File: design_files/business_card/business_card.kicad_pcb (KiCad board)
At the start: 2 copper layers, 85 x 55 mm, 35 parts, among them J1 Conn_01x06, J2 Conn_01x04_Male, SW1 SW_Push, SW2 SW_Push, SW3 SW_Push, SW4 SW_Push, U1 ATTINY85-20SU, U2 TLC5940PWP

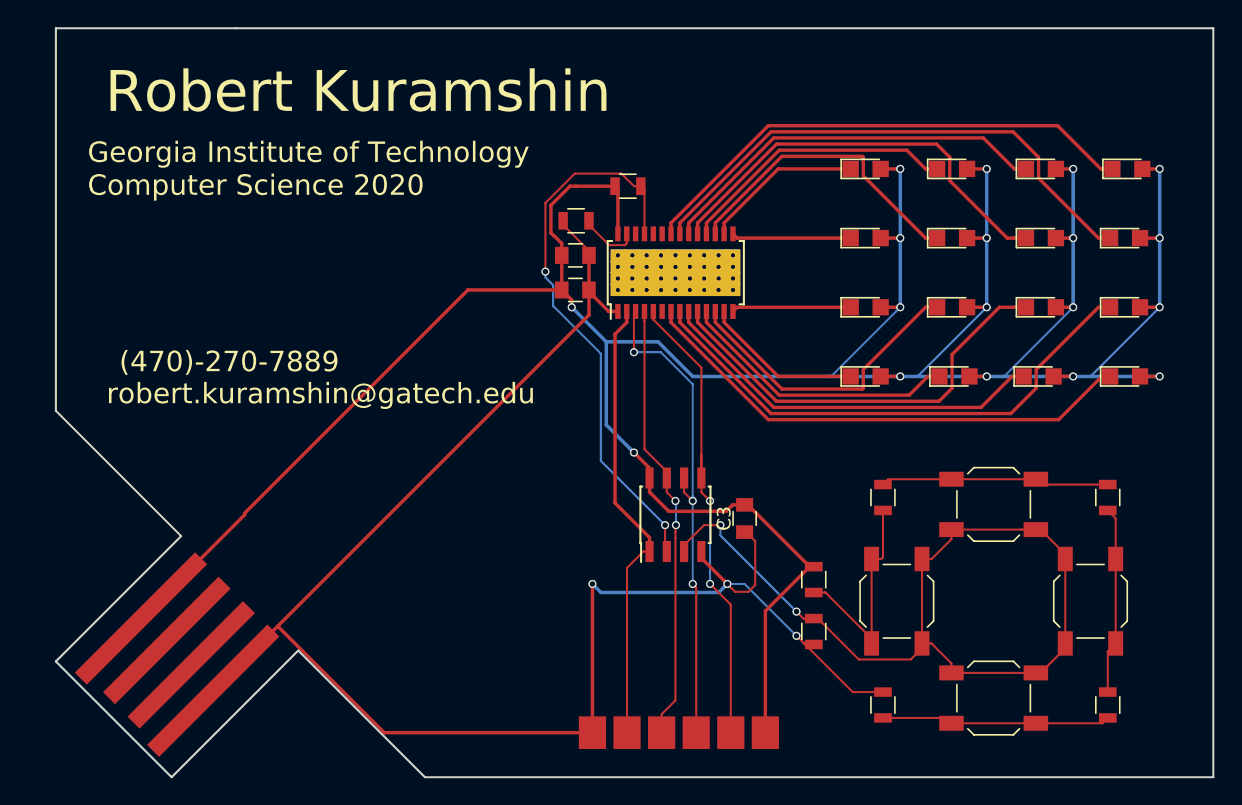
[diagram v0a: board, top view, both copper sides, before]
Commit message: progress on configuring 15 leds
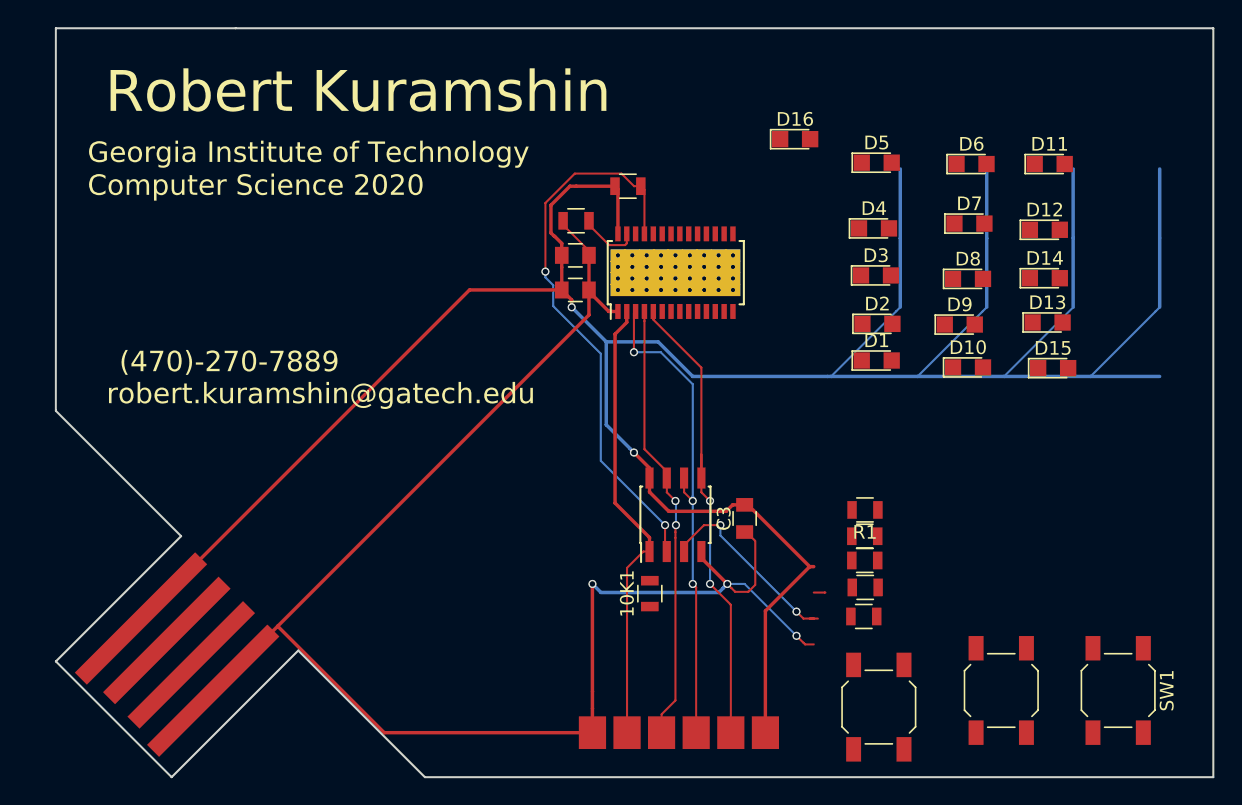
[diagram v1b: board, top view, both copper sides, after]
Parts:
- removed R2: 8.2K, Resistors_SMD:R_0805
- removed SW2: SW_Push, Buttons_Switches_SMD:SW_SPST_SKQG
- added 10K1: R, Resistors_SMD:R_0805, F.Cu at (188.6, 131.5)
- R1: value 16K -> 8K
- moved D16 24.5 mm to (199.3, 98.1)
- moved R4 20.8 mm to (204.4, 129.1), turned to 180 degrees
- moved D1 18.3 mm to (205.3, 114.4)
- moved D2 18.2 mm to (205.3, 111.7)
- moved R3 18.1 mm to (204.4, 127.3), turned to 0 degrees
- moved SW1 17.5 mm to (223.0, 138.6), turned to 270 degrees
- moved D5 16.7 mm to (205.3, 99.9)
- moved D10 16.4 mm to (212.0, 114.9)
- moved D3 14.1 mm to (205.2, 108.2)
- moved D7 13.6 mm to (212.1, 104.3)
- moved D4 13.6 mm to (205.1, 104.7)
- moved D15 10.9 mm to (218.2, 115.0)
- moved D6 10.6 mm to (212.2, 100.0)
- moved D9 9.38 mm to (211.4, 111.8)
- moved SW3 9.27 mm to (214.4, 138.6), turned to 90 degrees
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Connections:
- J1 pad 2: BLANK -> Net-(10K1-Pad1)
- J1 pad 4: XLAT -> SDA
- J1 pad 5: SDA -> BLANK
- R3 pad 2: Net-(R2-Pad1) -> Net-(R1-Pad1)
- R6 pad 1: BTNS -> Net-(R6-Pad1)
- R8 pad 2: GSCLK -> Net-(R8-Pad2)
- SW3 pad 2: BTNS -> Net-(R6-Pad1)
- SW4 pad 2: BTNS -> Net-(R6-Pad1)
- U1 pad 1: BLANK -> Net-(10K1-Pad1)
- U1 pad 2: GSCLK -> BTNS
- U1 pad 3: BTNS -> Net-(U1-Pad3)
- U1 pad 5: SDA -> BLANK
- U1 pad 6: XLAT -> SDA
- U2 pad 25: GSCLK -> SCLK
- U2 pad 3: XLAT -> BLANK
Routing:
- net BLANK: track 34.4 -> 77.4 mm, vias 0 -> 4
- net GSCLK: track 41.7 -> 0.00 mm, vias 2 -> 0
- net Net-(D15-Pad1): track 39.3 -> 0.00 mm
- net Net-(D2-Pad1): track 39.2 -> 0.00 mm
- net Net-(D16-Pad1): track 37.5 -> 0.00 mm
- net Net-(D1-Pad1): track 37.3 -> 0.00 mm
- net XLAT: track 36.7 -> 0.00 mm, vias 3 -> 0
- net BTNS: track 62.3 -> 29.8 mm
- net Net-(D4-Pad1): track 32.5 -> 0.00 mm
- net Net-(D13-Pad1): track 32.0 -> 0.00 mm
- net Net-(D14-Pad1): track 29.1 -> 0.00 mm
- net Net-(D3-Pad1): track 28.9 -> 0.00 mm
- net Net-(D6-Pad1): track 22.4 -> 0.00 mm
- net Net-(D11-Pad1): track 22.4 -> 0.00 mm
- net VCC: track 237.1 -> 214.8 mm, vias 18 -> 2
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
